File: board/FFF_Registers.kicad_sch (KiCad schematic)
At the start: 16 parts, among them U1 74F573, U14 74F32, U18 74F02, U2 74F541, U46 74F32, U47 74F573, U48 74F541, U49 74F573, U50 74F541

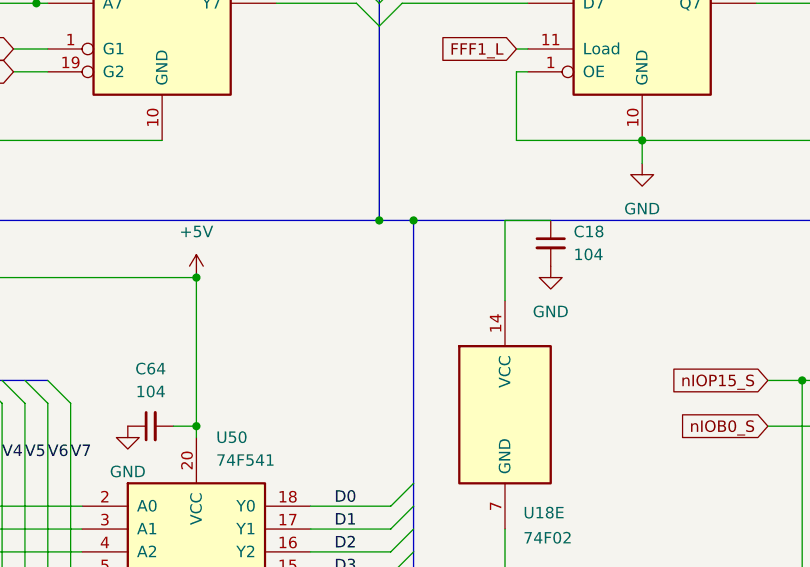
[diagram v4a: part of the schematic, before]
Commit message: Initial production breakout card and main PCB versions
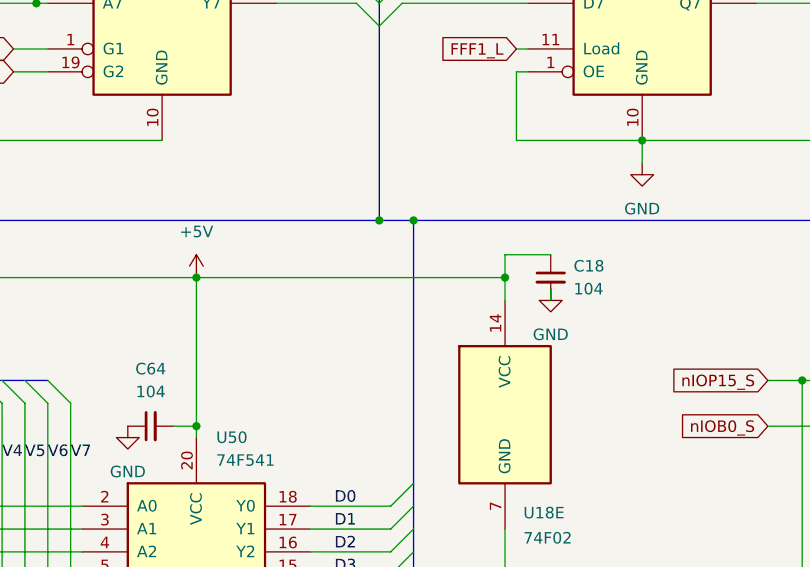
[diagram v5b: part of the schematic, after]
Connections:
- net +5V: now also C18.1, U18.14 (VCC)
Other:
- moved on the sheet: C18
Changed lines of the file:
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@@
 		(title "FFFx Registers and Logic")
 		(date "2024-10-09")
-		(rev "0.1A")
+		(rev "0.3B")
 		(company "Data Tuning")
 		(comment 1 "Hydra 16")
@@
 	)
 	(junction
+		(at 140.97 90.17)
+		(diameter 0)
+		(color 0 0 0 0)
+	)
+	(junction
 		(at 60.96 106.68)
 		(diameter 0)
@@
 	(wire
 		(pts
-			(xy 140.97 83.82) (xy 146.05 83.82)
+			(xy 140.97 87.63) (xy 146.05 87.63)
 		)
 		(stroke
@@
 		)
 	)
-	(bus
-		(pts
-			(xy 226.06 62.23) (xy 226.06 83.82)
-		)
-		(stroke
-			(width 0)
-			(type default)
-		)
-	)
 	(wire
 		(pts
@@
 		)
 	)
-	(bus
-		(pts
-			(xy 130.81 83.82) (xy 226.06 83.82)
-		)
-		(stroke
-			(width 0)
-			(type default)
-		)
-	)
 	(wire
 		(pts
@@
 		)
 	)
+	(bus
+		(pts
+			(xy 130.81 83.82) (xy 226.06 83.82)
+		)
+		(stroke
+			(width 0)
+			(type default)
+		)
+	)
 	(wire
 		(pts
@@
 		)
 	)
+	(wire
+		(pts
+			(xy 146.05 91.44) (xy 146.05 92.71)
+		)
+		(stroke
+			(width 0)
+			(type default)
+		)
+	)
 	(bus
 		(pts
@@
 	(wire
 		(pts
+			(xy 140.97 90.17) (xy 140.97 92.71)
+		)
+		(stroke
+			(width 0)
+			(type default)
+		)
+	)
+	(wire
+		(pts
 			(xy 74.93 115.57) (xy 93.98 115.57)
 		)
@@
 	(wire
 		(pts
+			(xy 106.68 90.17) (xy 140.97 90.17)
+		)
+		(stroke
+			(width 0)
+			(type default)
+		)
+	)
+	(wire
+		(pts
 			(xy 187.96 59.69) (xy 189.23 59.69)
 		)
@@
 		)
 	)
+	(bus
+		(pts
+			(xy 226.06 62.23) (xy 226.06 83.82)
+		)
+		(stroke
+			(width 0)
+			(type default)
+		)
+	)
 	(wire
 		(pts
@@
 	(wire
 		(pts
-			(xy 140.97 83.82) (xy 140.97 92.71)
+			(xy 140.97 87.63) (xy 140.97 90.17)
 		)
 		(stroke
@@
 	(symbol
 		(lib_id "Device:C_Small")
-		(at 146.05 86.36 0)
+		(at 146.05 90.17 0)
 		(unit 1)
 		(exclude_from_sim no)
@@
 		(fields_autoplaced yes)
 		(property "Reference" "C18"
-			(at 148.59 85.0962 0)
+			(at 148.59 88.9062 0)
 			(effects
 				(font
@@
 		)
 		(property "Value" "104"
-			(at 148.59 87.6362 0)
+			(at 148.59 91.4462 0)
 			(effects
 				(font
@@
 		)
 		(property "Footprint" "Capacitor_THT:C_Disc_D5.0mm_W2.5mm_P5.00mm"
-			(at 146.05 86.36 0)
+			(at 146.05 90.17 0)
 			(effects
 				(font
@@
 		)
 		(property "Datasheet" "~"
-			(at 146.05 86.36 0)
+			(at 146.05 90.17 0)
 			(effects
 				(font
@@
 		)
 		(property "Description" "Unpolarized capacitor, small symbol"
-			(at 146.05 86.36 0)
+			(at 146.05 90.17 0)
 			(effects
 				(font
@@
 	(symbol
 		(lib_id "power:GND")
-		(at 146.05 88.9 0)
+		(at 146.05 91.44 0)
 		(unit 1)
 		(exclude_from_sim no)
@@
 		(fields_autoplaced yes)
 		(property "Reference" "#PWR018"
-			(at 146.05 95.25 0)
+			(at 146.05 97.79 0)
 			(effects
 				(font
@@
 		)
 		(property "Value" "GND"
-			(at 146.05 93.98 0)
+			(at 146.05 96.52 0)
 			(effects
 				(font
@@
 		)
 		(property "Footprint" ""
-			(at 146.05 88.9 0)
+			(at 146.05 91.44 0)
 			(effects
 				(font
@@
 		)
 		(property "Datasheet" ""
-			(at 146.05 88.9 0)
+			(at 146.05 91.44 0)
 			(effects
 				(font
@@
 		)
 		(property "Description" "Power symbol creates a global label with name \"GND\" , ground"
-			(at 146.05 88.9 0)
+			(at 146.05 91.44 0)
 			(effects
 				(font

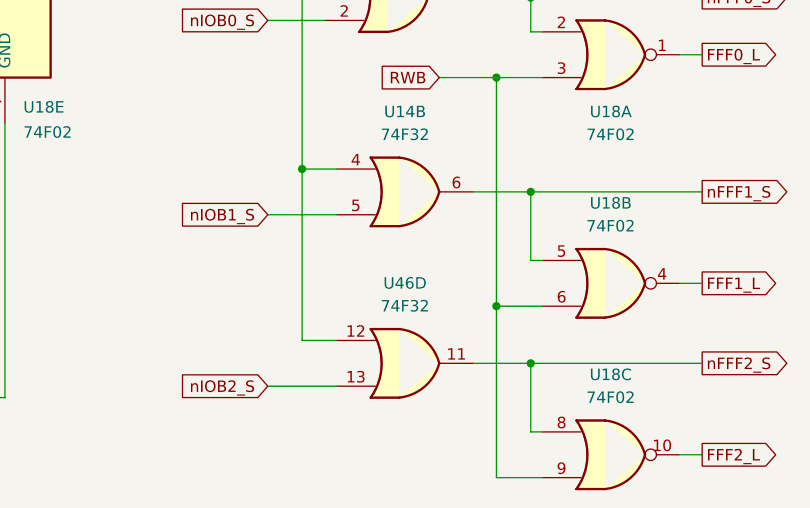
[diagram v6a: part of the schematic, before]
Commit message: Version 0.5A of main board and updates to ROM code to match latest changes.
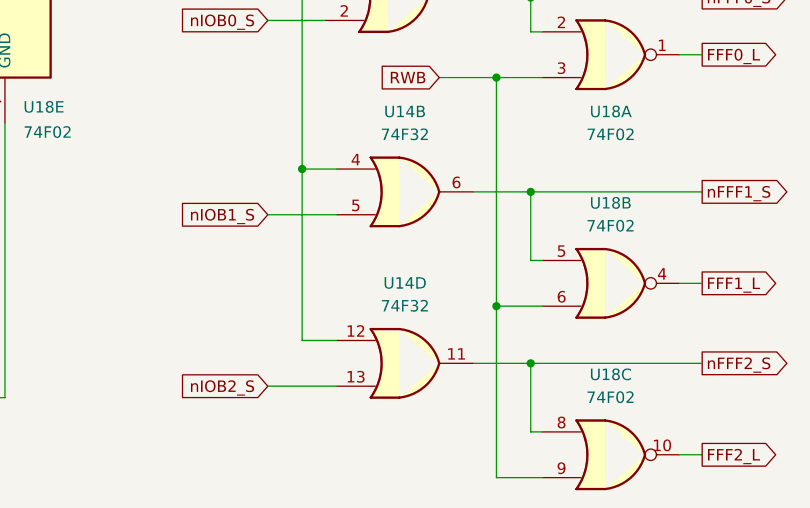
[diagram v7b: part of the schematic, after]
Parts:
- removed U46: 74F32, Package_DIP:DIP-14_W7.62mm_Socket_LongPads, symbol 74xx:74LS32
- added unit 4 of U14
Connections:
- net nFFF2_S: now also U14.11
- net nIOB2_S: now also U14.13
- net nIOP15_S: now also U14.12
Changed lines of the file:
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@@
 		(title "FFFx Registers and Logic")
 		(date "2024-10-21")
-		(rev "0.4A")
+		(rev "0.5A")
 		(company "Data Tuning")
 		(comment 1 "Hydra 16")
@@
 	(symbol
 		(lib_id "74xx:74LS32")
-		(at 185.42 144.78 0)
-		(unit 4)
-		(exclude_from_sim no)
-		(in_bom yes)
-		(on_board yes)
-		(dnp no)
-		(property "Reference" "U46"
-			(at 185.42 135.89 0)
-			(effects
-				(font
-					(size 1.27 1.27)
-				)
-			)
-		)
-		(property "Value" "74F32"
-			(at 185.42 138.43 0)
-			(effects
-				(font
-					(size 1.27 1.27)
-				)
-			)
-		)
-		(property "Footprint" "Package_DIP:DIP-14_W7.62mm_Socket_LongPads"
-			(at 185.42 144.78 0)
-			(effects
-				(font
-					(size 1.27 1.27)
-				)
-				(hide yes)
-			)
-		)
-		(property "Datasheet" "http://www.ti.com/lit/gpn/sn74LS32"
-			(at 185.42 144.78 0)
-			(effects
-				(font
-					(size 1.27 1.27)
-				)
-				(hide yes)
-			)
-		)
-		(property "Description" "Quad 2-input OR"
-			(at 185.42 144.78 0)
-			(effects
-				(font
-					(size 1.27 1.27)
-				)
-				(hide yes)
-			)
-		)
-		(pin "10"
-		)
-		(pin "3"
-		)
-		(pin "11"
-		)
-		(pin "12"
-		)
-		(pin "2"
-		)
-		(pin "1"
-		)
-		(pin "14"
-		)
-		(pin "13"
-		)
-		(pin "4"
-		)
-		(pin "9"
-		)
-		(pin "7"
-		)
-		(pin "5"
-		)
-		(pin "6"
-		)
-		(pin "8"
-		)
-		(instances
-			(project "hydra-16"
-				(path "/ef29fc71-3fec-48b5-8a1a-46bee537a98c/9c3f9893-75ea-4823-afb7-35bb324a2c9f"
-					(reference "U46")
-					(unit 4)
-				)
-			)
-		)
-	)
-	(symbol
-		(lib_id "74xx:74LS32")
 		(at 184.15 104.14 0)
 		(unit 1)
@@
 				)
 			)
+		)
+	)
+	(symbol
+		(lib_id "74xx:74LS32")
+		(at 185.42 144.78 0)
+		(unit 4)
+		(exclude_from_sim no)
+		(in_bom yes)
+		(on_board yes)
+		(dnp no)
+		(fields_autoplaced yes)
+		(property "Reference" "U14"
+			(at 185.42 135.89 0)
+			(effects
+				(font
+					(size 1.27 1.27)
+				)
+			)
+		)
+		(property "Value" "74F32"
+			(at 185.42 138.43 0)
+			(effects
+				(font
+					(size 1.27 1.27)
+				)
+			)
+		)
+		(property "Footprint" "Package_DIP:DIP-14_W7.62mm_Socket_LongPads"
+			(at 185.42 144.78 0)
+			(effects
+				(font
+					(size 1.27 1.27)
+				)
+				(hide yes)
+			)
+		)
+		(property "Datasheet" "http://www.ti.com/lit/gpn/sn74LS32"
+			(at 185.42 144.78 0)
+			(effects
+				(font
+					(size 1.27 1.27)
+				)
+				(hide yes)
+			)
+		)
+		(property "Description" "Quad 2-input OR"
+			(at 185.42 144.78 0)
+			(effects
+				(font
+					(size 1.27 1.27)
+				)
+				(hide yes)
+			)
+		)
+		(pin "10"
+		)
+		(pin "3"
+		)
+		(pin "11"
+		)
+		(pin "12"
+		)
+		(pin "2"
+		)
+		(pin "1"
+		)
+		(pin "14"
+		)
+		(pin "13"
+		)
+		(pin "4"
+		)
+		(pin "9"
+		)
+		(pin "7"
+		)
+		(pin "5"
+		)
+		(pin "6"
+		)
+		(pin "8"
+		)
+		(instances
+			(project "hydra-16"
+				(path "/ef29fc71-3fec-48b5-8a1a-46bee537a98c/9c3f9893-75ea-4823-afb7-35bb324a2c9f"
+					(reference "U14")
+					(unit 4)
+				)
+			)
